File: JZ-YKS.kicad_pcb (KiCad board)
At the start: 2 copper layers, 50 x 50 mm, 38 parts, among them IC1 JZ4725, X1 X1, X2 X2

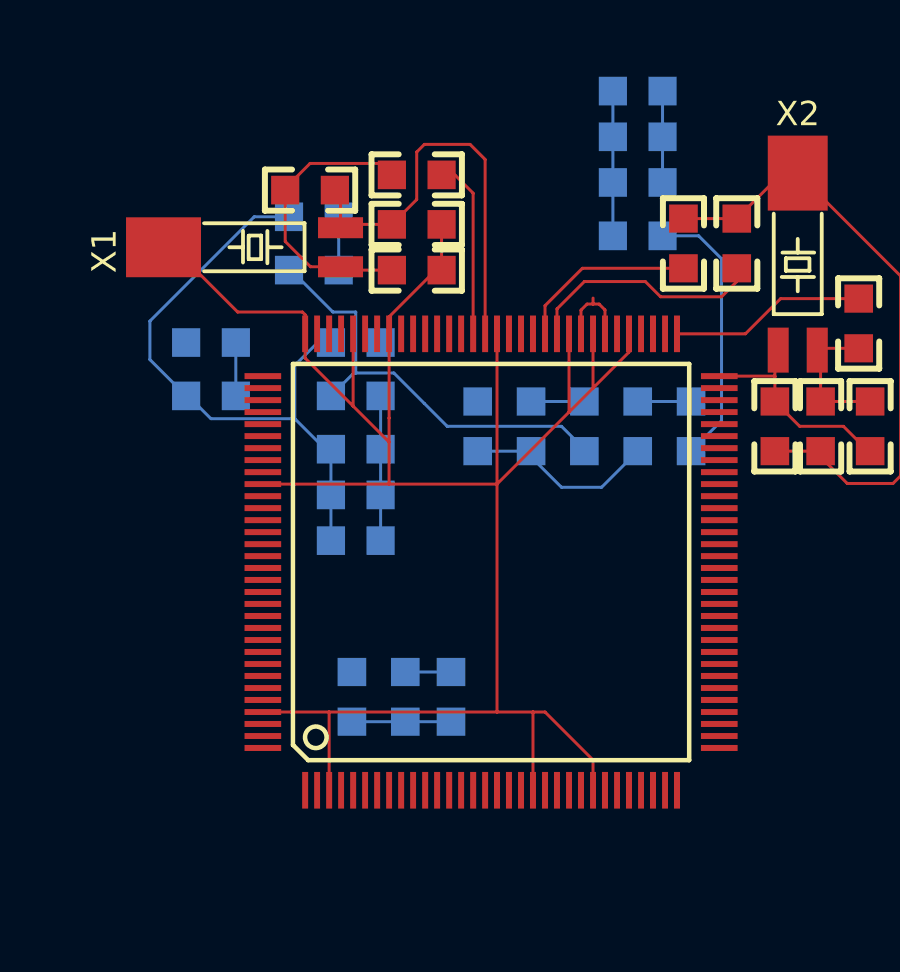
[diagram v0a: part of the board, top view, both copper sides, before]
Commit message: added some vias
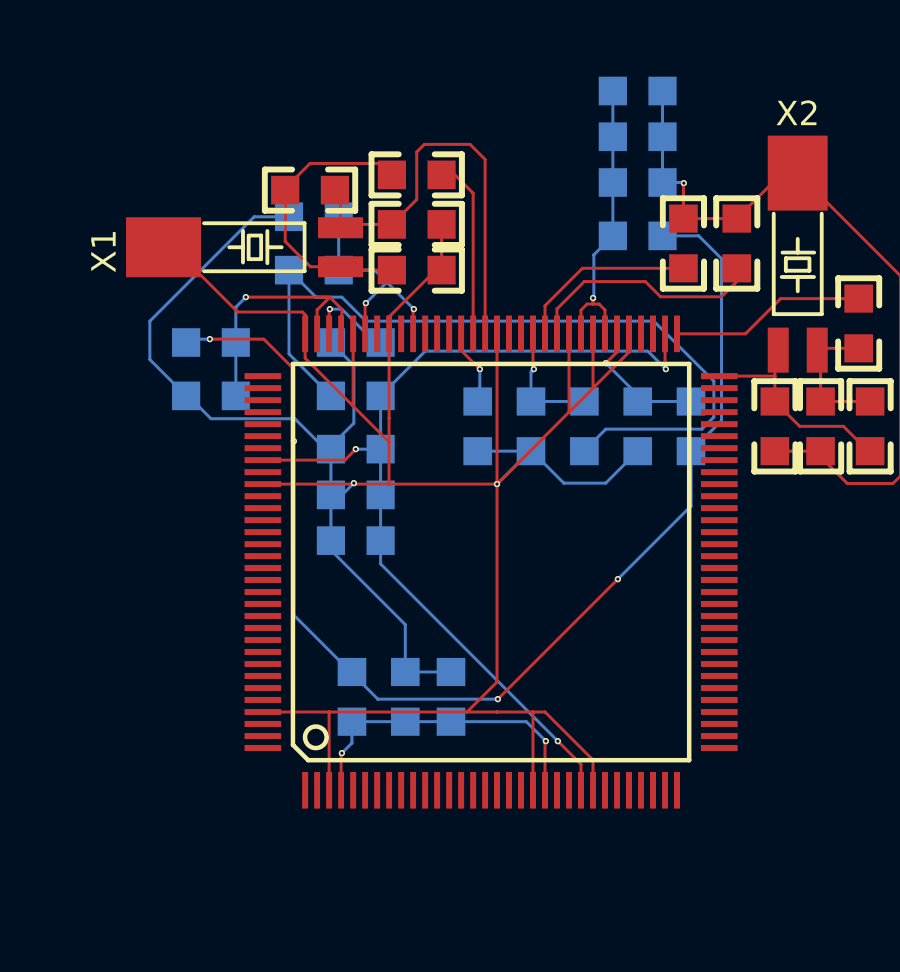
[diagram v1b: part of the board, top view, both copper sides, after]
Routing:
- net +1.8V: track 9.12 -> 40.3 mm, vias 0 -> 4
- net N-00000103: track 4.83 -> 31.6 mm, vias 0 -> 3
- net +3.3V: track 14.7 -> 26.5 mm
- net GND: track 125.3 -> 136.3 mm, vias 0 -> 3
- net N-00000104: track 3.30 -> 10.8 mm, vias 0 -> 2
- net N-000004: track 1.78 -> 9.03 mm, vias 0 -> 1
- net N-0000013: track 1.78 -> 7.82 mm, vias 0 -> 2
- net N-0000010: track 0.00 -> 2.99 mm, vias 0 -> 1
- net N-0000011: track 1.78 -> 4.63 mm, vias 0 -> 1
- net VRTC: track 0.00 -> 2.54 mm, vias 0 -> 1
- net N-0000080: track 7.58 -> 9.92 mm, vias 0 -> 1
- net N-0000012: track 1.78 -> 4.08 mm, vias 0 -> 1

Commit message: no more testpoints
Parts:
- removed TP1, TP2, TP3, TP4: TP, TP40x20
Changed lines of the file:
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@@
 (kicad_pcb (version 3) (host pcbnew "(2013-mar-13)-testing")
   (general
-    (links 85)
-    (no_connects 5)
+    (links 81)
+    (no_connects 1)
     (area 186.698999 110.355 245.946619 166.505001)
     (thickness 1.6)
@@
     (tracks 279)
     (zones 0)
-    (modules 38)
+    (modules 34)
     (nets 21)
   )
@@
     (add_net VRTC)
   )
-  (module TP40x20 (layer F.Cu)
-    (at 232.537 145.034)
-    (fp_text reference TP4 (at 0 -2.54) (layer F.SilkS) hide
-      (effects (font (thickness 0.3048)))
-    )
-    (fp_text value TP (at 0 2.54) (layer F.SilkS) hide
-      (effects (font (thickness 0.3048)))
-    )
-    (pad 1 smd oval (at 0 0) (size 1.016 0.508)
-      (layers F.Cu F.Paste F.Mask)
-      (net 2 +3.3V)
-    )
-  )
-  (module TP40x20 (layer F.Cu)
-    (at 232.537 143.764)
-    (fp_text reference TP3 (at 0 -2.54) (layer F.SilkS) hide
-      (effects (font (thickness 0.3048)))
-    )
-    (fp_text value TP (at 0 2.54) (layer F.SilkS) hide
-      (effects (font (thickness 0.3048)))
-    )
-    (pad 1 smd oval (at 0 0) (size 1.016 0.508)
-      (layers F.Cu F.Paste F.Mask)
-      (net 1 +1.8V)
-    )
-  )
-  (module TP40x20 (layer F.Cu)
-    (at 232.537 142.494)
-    (fp_text reference TP2 (at 0 -2.54) (layer F.SilkS) hide
-      (effects (font (thickness 0.3048)))
-    )
-    (fp_text value TP (at 0 2.54) (layer F.SilkS) hide
-      (effects (font (thickness 0.3048)))
-    )
-    (pad 1 smd oval (at 0 0) (size 1.016 0.508)
-      (layers F.Cu F.Paste F.Mask)
-      (net 20 VRTC)
-    )
-  )
-  (module TP40x20 (layer F.Cu)
-    (at 232.537 146.304)
-    (fp_text reference TP1 (at 0 -2.54) (layer F.SilkS) hide
-      (effects (font (thickness 0.3048)))
-    )
-    (fp_text value TP (at 0 2.54) (layer F.SilkS) hide
-      (effects (font (thickness 0.3048)))
-    )
-    (pad 1 smd oval (at 0 0) (size 1.016 0.508)
-      (layers F.Cu F.Paste F.Mask)
-      (net 3 GND)
-    )
-  )
   (module size-0603 (layer F.Cu)
     (at 218.186 130.81 90)
@@
     (arrow2b (pts (xy 186.774 112.430001) (xy 187.900503 111.843581)))
   )
-  (segment (start 207.137 145.09496) (end 207.09496 145.09496) (width 0.1) (layer B.Cu) (net 1) (status C00000))
-  (segment (start 201.888 134.112) (end 201.60996 134.112) (width 0.1) (layer B.Cu) (net 1) (status C00000))
-  (segment (start 202 134) (end 201.888 134.112) (width 0.1) (layer B.Cu) (net 1) (status C00000))
-  (segment (start 202.4 134) (end 202 134) (width 0.1) (layer B.Cu) (net 1) (status 800000))
+  (segment (start 207.137 145.09496) (end 207.09496 145.09496) (width 0.1) (layer B.Cu) (net 1))
+  (segment (start 201.888 134.112) (end 201.60996 134.112) (width 0.1) (layer B.Cu) (net 1))
+  (segment (start 202 134) (end 201.888 134.112) (width 0.1) (layer B.Cu) (net 1))
+  (segment (start 202.4 134) (end 202 134) (width 0.1) (layer B.Cu) (net 1))
   (via (at 202.4 134) (size 0.21) (layers F.Cu B.Cu) (net 1))
   (segment (start 204.2 134) (end 202.4 134) (width 0.1) (layer F.Cu) (net 1))
@@
   (via (at 205.2 137.4) (size 0.21) (layers F.Cu B.Cu) (net 1))
   (segment (start 205.2 143.2) (end 205.2 137.4) (width 0.1) (layer B.Cu) (net 1))
-  (segment (start 207.09496 145.09496) (end 205.2 143.2) (width 0.1) (layer B.Cu) (net 1) (status 400000))
-  (segment (start 207.137 145.09496) (end 207.137 145.137) (width 0.1) (layer B.Cu) (net 1) (status C00000))
-  (segment (start 218.44 139.56) (end 218.44 137.73404) (width 0.1) (layer B.Cu) (net 1) (status 800000))
+  (segment (start 207.09496 145.09496) (end 205.2 143.2) (width 0.1) (layer B.Cu) (net 1))
+  (segment (start 207.137 145.09496) (end 207.137 145.137) (width 0.1) (layer B.Cu) (net 1))
+  (segment (start 218.44 139.56) (end 218.44 137.73404) (width 0.1) (layer B.Cu) (net 1))
   (segment (start 216 142) (end 218.44 139.56) (width 0.1) (layer B.Cu) (net 1))
   (via (at 216 142) (size 0.21) (layers F.Cu B.Cu) (net 1))
@@
   (via (at 212 146) (size 0.21) (layers F.Cu B.Cu) (net 1))
   (segment (start 208 146) (end 212 146) (width 0.1) (layer B.Cu) (net 1))
-  (segment (start 207.137 145.137) (end 208 146) (width 0.1) (layer B.Cu) (net 1) (status 400000))
+  (segment (start 207.137 145.137) (end 208 146) (width 0.1) (layer B.Cu) (net 1))
   (segment (start 217.49004 130.556) (end 218.694 130.556) (width 0.1) (layer B.Cu) (net 1))
   (segment (start 219.456 136.71804) (end 218.44 137.73404) (width 0.1) (layer B.Cu) (net 1))
   (segment (start 219.456 131.318) (end 219.456 136.71804) (width 0.1) (layer B.Cu) (net 1))
   (segment (start 218.694 130.556) (end 219.456 131.318) (width 0.1) (layer B.Cu) (net 1))
-  (segment (start 214.884 137.73404) (end 214.884 137.716) (width 0.1) (layer B.Cu) (net 2) (status C00000))
-  (segment (start 205.93996 132.6) (end 205.03896 131.699) (width 0.1) (layer B.Cu) (net 2) (status 800000))
+  (segment (start 214.884 137.73404) (end 214.884 137.716) (width 0.1) (layer B.Cu) (net 2))
+  (segment (start 205.93996 132.6) (end 205.03896 131.699) (width 0.1) (layer B.Cu) (net 2))
   (segment (start 206.8 132.6) (end 205.93996 132.6) (width 0.1) (layer B.Cu) (net 2))
   (segment (start 207.6 133.4) (end 206.8 132.6) (width 0.1) (layer B.Cu) (net 2))
@@
   (segment (start 218.8 137) (end 219.2 136.6) (width 0.1) (layer B.Cu) (net 2))
   (segment (start 215.6 137) (end 218.8 137) (width 0.1) (layer B.Cu) (net 2))
-  (segment (start 214.884 137.716) (end 215.6 137) (width 0.1) (layer B.Cu) (net 2) (status 400000))
-  (segment (start 205.03896 131.699) (end 205.03896 134.493) (width 0.1) (layer B.Cu) (net 2) (status 400000))
-  (segment (start 205.03896 134.493) (end 206.43596 135.89) (width 0.1) (layer B.Cu) (net 2) (status 800000))
+  (segment (start 214.884 137.716) (end 215.6 137) (width 0.1) (layer B.Cu) (net 2))
+  (segment (start 205.03896 131.699) (end 205.03896 134.493) (width 0.1) (layer B.Cu) (net 2))
+  (segment (start 205.03896 134.493) (end 206.43596 135.89) (width 0.1) (layer B.Cu) (net 2))
   (segment (start 211.97242 138.83158) (end 211.97242 145.42758) (width 0.1) (layer F.Cu) (net 3))
   (segment (start 211.97242 145.42758) (end 210.97128 146.42872) (width 0.1) (layer F.Cu) (net 3))
-  (segment (start 213.106 137.73404) (end 213.13404 137.73404) (width 0.1) (layer B.Cu) (net 3) (status C00000))
-  (segment (start 215.59604 138.8) (end 216.662 137.73404) (width 0.1) (layer B.Cu) (net 3) (status 800000))
+  (segment (start 213.106 137.73404) (end 213.13404 137.73404) (width 0.1) (layer B.Cu) (net 3))
+  (segment (start 215.59604 138.8) (end 216.662 137.73404) (width 0.1) (layer B.Cu) (net 3))
   (segment (start 214.2 138.8) (end 215.59604 138.8) (width 0.1) (layer B.Cu) (net 3))
-  (segment (start 213.13404 137.73404) (end 214.2 138.8) (width 0.1) (layer B.Cu) (net 3) (status 400000))
-  (segment (start 206.43596 137.668) (end 206.43596 137.56404) (width 0.1) (layer B.Cu) (net 3) (status C00000))
-  (segment (start 207.2 134.87604) (end 206.43596 134.112) (width 0.1) (layer B.Cu) (net 3) (status 800000))
+  (segment (start 213.13404 137.73404) (end 214.2 138.8) (width 0.1) (layer B.Cu) (net 3))
+  (segment (start 206.43596 137.668) (end 206.43596 137.56404) (width 0.1) (layer B.Cu) (net 3))
+  (segment (start 207.2 134.87604) (end 206.43596 134.112) (width 0.1) (layer B.Cu) (net 3))
   (segment (start 207.2 136.8) (end 207.2 134.87604) (width 0.1) (layer B.Cu) (net 3))
-  (segment (start 206.43596 137.56404) (end 207.2 136.8) (width 0.1) (layer B.Cu) (net 3) (status 400000))
+  (segment (start 206.43596 137.56404) (end 207.2 136.8) (width 0.1) (layer B.Cu) (net 3))
   (segment (start 206.43596 139.192) (end 206.808 139.192) (width 0.1) (layer B.Cu) (net 3))
   (segment (start 207.2 138.8) (end 207.2 138.83158) (width 0.1) (layer F.Cu) (net 3))

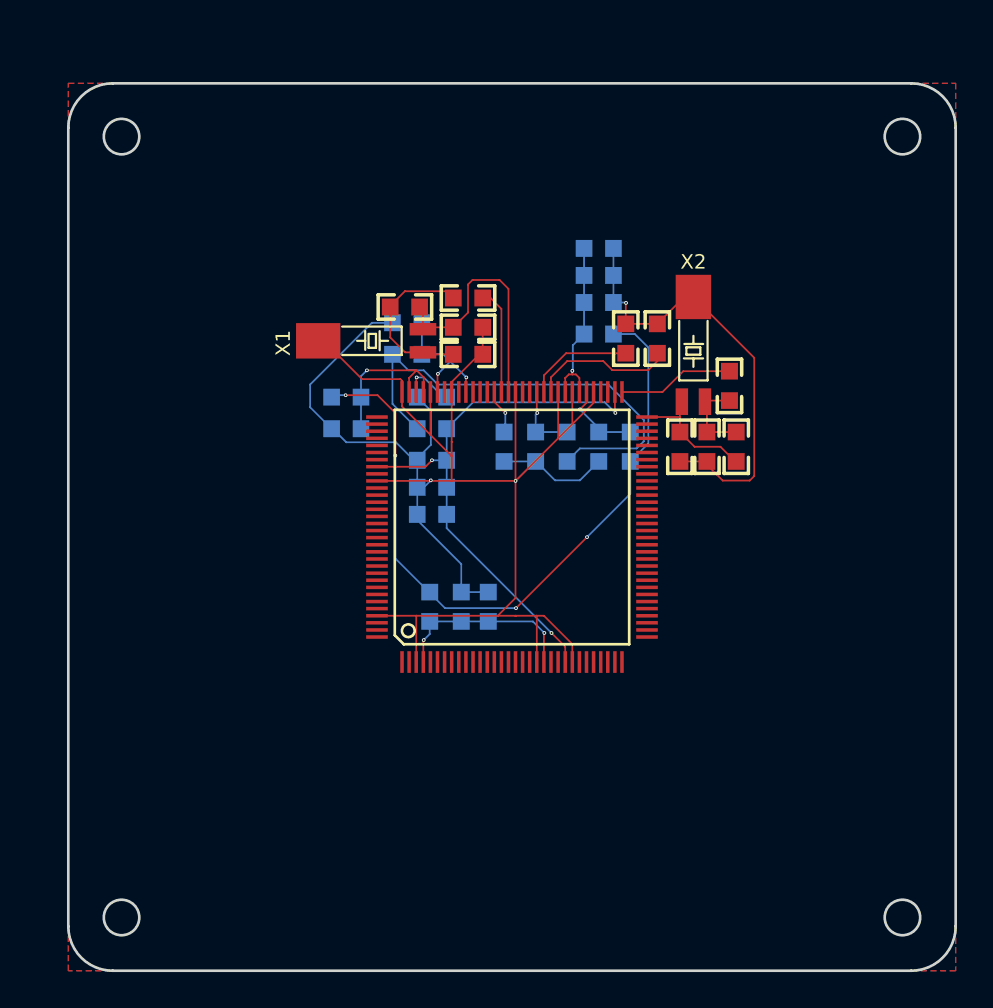
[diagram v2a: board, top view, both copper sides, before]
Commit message: lcd and i2c/uart connectors
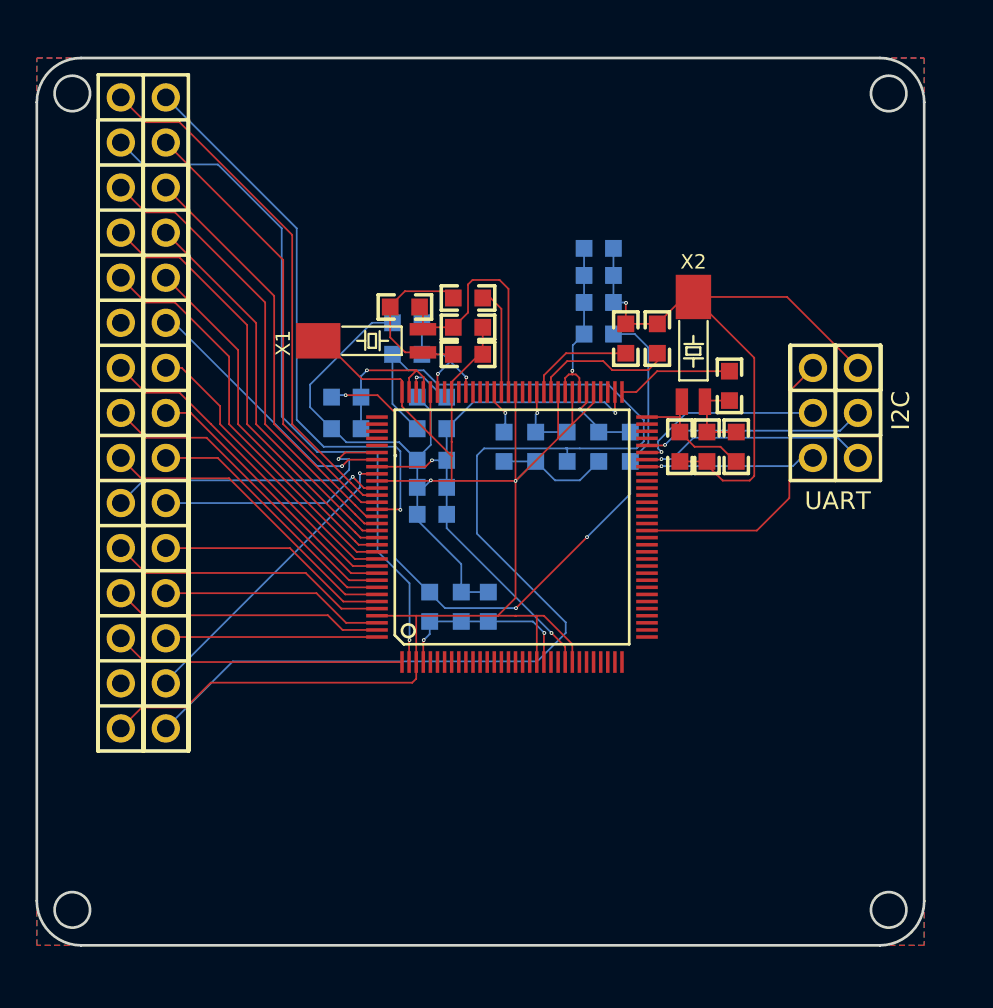
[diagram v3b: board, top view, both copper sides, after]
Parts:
- added ?: PINHEAD6, pinhead-double-2.54mm-6, F.Cu at (230.0, 135.0)
- added U1: PINHEAD30, pinhead-double-2.54mm-30, F.Cu at (191.0, 135.0)
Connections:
- IC1 pad 1: (no net) -> B2
- IC1 pad 102: (no net) -> G0
- IC1 pad 103: (no net) -> R1
- IC1 pad 105: (no net) -> B1
- IC1 pad 107: (no net) -> G1
- IC1 pad 108: (no net) -> VSYN
- IC1 pad 109: (no net) -> HSYN
- IC1 pad 110: (no net) -> DE
- IC1 pad 111: (no net) -> R7
- IC1 pad 112: (no net) -> R6
- IC1 pad 113: (no net) -> R5
- IC1 pad 114: (no net) -> R4
- IC1 pad 115: (no net) -> R3
- IC1 pad 116: (no net) -> R2
- IC1 pad 117: (no net) -> G7
- IC1 pad 118: (no net) -> G6
- IC1 pad 119: (no net) -> G5
- IC1 pad 120: (no net) -> G4
- IC1 pad 121: (no net) -> G3
- IC1 pad 122: (no net) -> G2
- IC1 pad 123: (no net) -> B7
- IC1 pad 124: (no net) -> B6
- IC1 pad 126: (no net) -> B5
- IC1 pad 127: (no net) -> B4
- IC1 pad 128: (no net) -> B3
- IC1 pad 2: (no net) -> PCLK
- IC1 pad 48: (no net) -> PWM
- IC1 pad 57: (no net) -> RXD
- IC1 pad 58: (no net) -> TXD
- IC1 pad 59: (no net) -> SCK
- IC1 pad 60: (no net) -> SDA
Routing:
- net +3.3V: track 26.5 -> 69.1 mm
- net PCLK: track 0.00 -> 40.5 mm, vias 0 -> 1
- net DE: track 0.00 -> 32.4 mm, vias 0 -> 1
- net VSYN: track 0.00 -> 30.0 mm
- net GND: track 136.3 -> 165.9 mm
- net R6: track 0.00 -> 26.3 mm
- net HSYN: track 0.00 -> 25.7 mm
- net R4: track 0.00 -> 24.8 mm
- net R7: track 0.00 -> 23.8 mm
- net R2: track 0.00 -> 23.1 mm
- net R5: track 0.00 -> 22.2 mm
- net R3: track 0.00 -> 20.6 mm
- net G6: track 0.00 -> 19.1 mm
- net G4: track 0.00 -> 18.3 mm
- net G2: track 0.00 -> 17.6 mm
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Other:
- outline, holes or cut-outs redrawn
- board text added: "I2C"
- board text added: "UART"

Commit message: audio connector
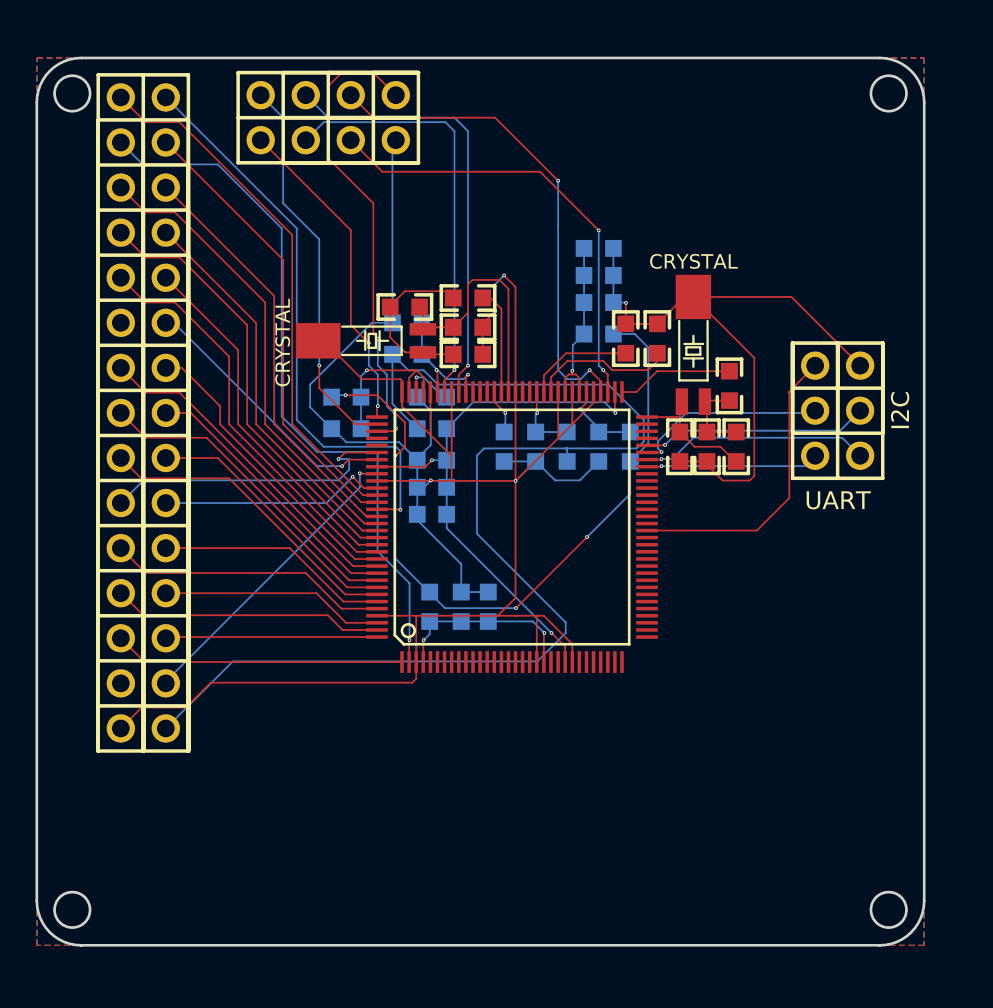
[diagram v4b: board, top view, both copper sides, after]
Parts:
- removed ?: PINHEAD6, pinhead-double-2.54mm-6
- added U2: PINHEAD6, pinhead-double-2.54mm-6, F.Cu at (230.1, 134.9)
- added U3: PINHEAD8, pinhead-double-2.54mm-8, F.Cu at (201.4, 118.4)
- X1: value X1 -> CRYSTAL
- X2: value X2 -> CRYSTAL
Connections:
- IC1 pad 67: (no net) -> ADIN0
- IC1 pad 68: (no net) -> ADIN1
- IC1 pad 88: (no net) -> HP_R
- IC1 pad 90: (no net) -> HP_L
- IC1 pad 97: (no net) -> IN_L
- IC1 pad 98: (no net) -> IN_R
- IC1 pad 99: (no net) -> MIC
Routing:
- net ADIN1: track 0.00 -> 28.0 mm, vias 0 -> 2
- net MIC: track 0.00 -> 26.7 mm, vias 0 -> 2
- net ADIN0: track 0.00 -> 25.4 mm, vias 0 -> 2
- net HP_R: track 0.00 -> 24.9 mm, vias 0 -> 1
- net HP_L: track 0.00 -> 23.9 mm, vias 0 -> 1
- net IN_R: track 0.00 -> 22.0 mm, vias 0 -> 1
- net IN_L: track 0.00 -> 18.4 mm, vias 0 -> 2
- net GND: track 165.9 -> 183.7 mm, vias 3 -> 5
